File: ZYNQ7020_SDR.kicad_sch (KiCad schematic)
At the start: 0 parts

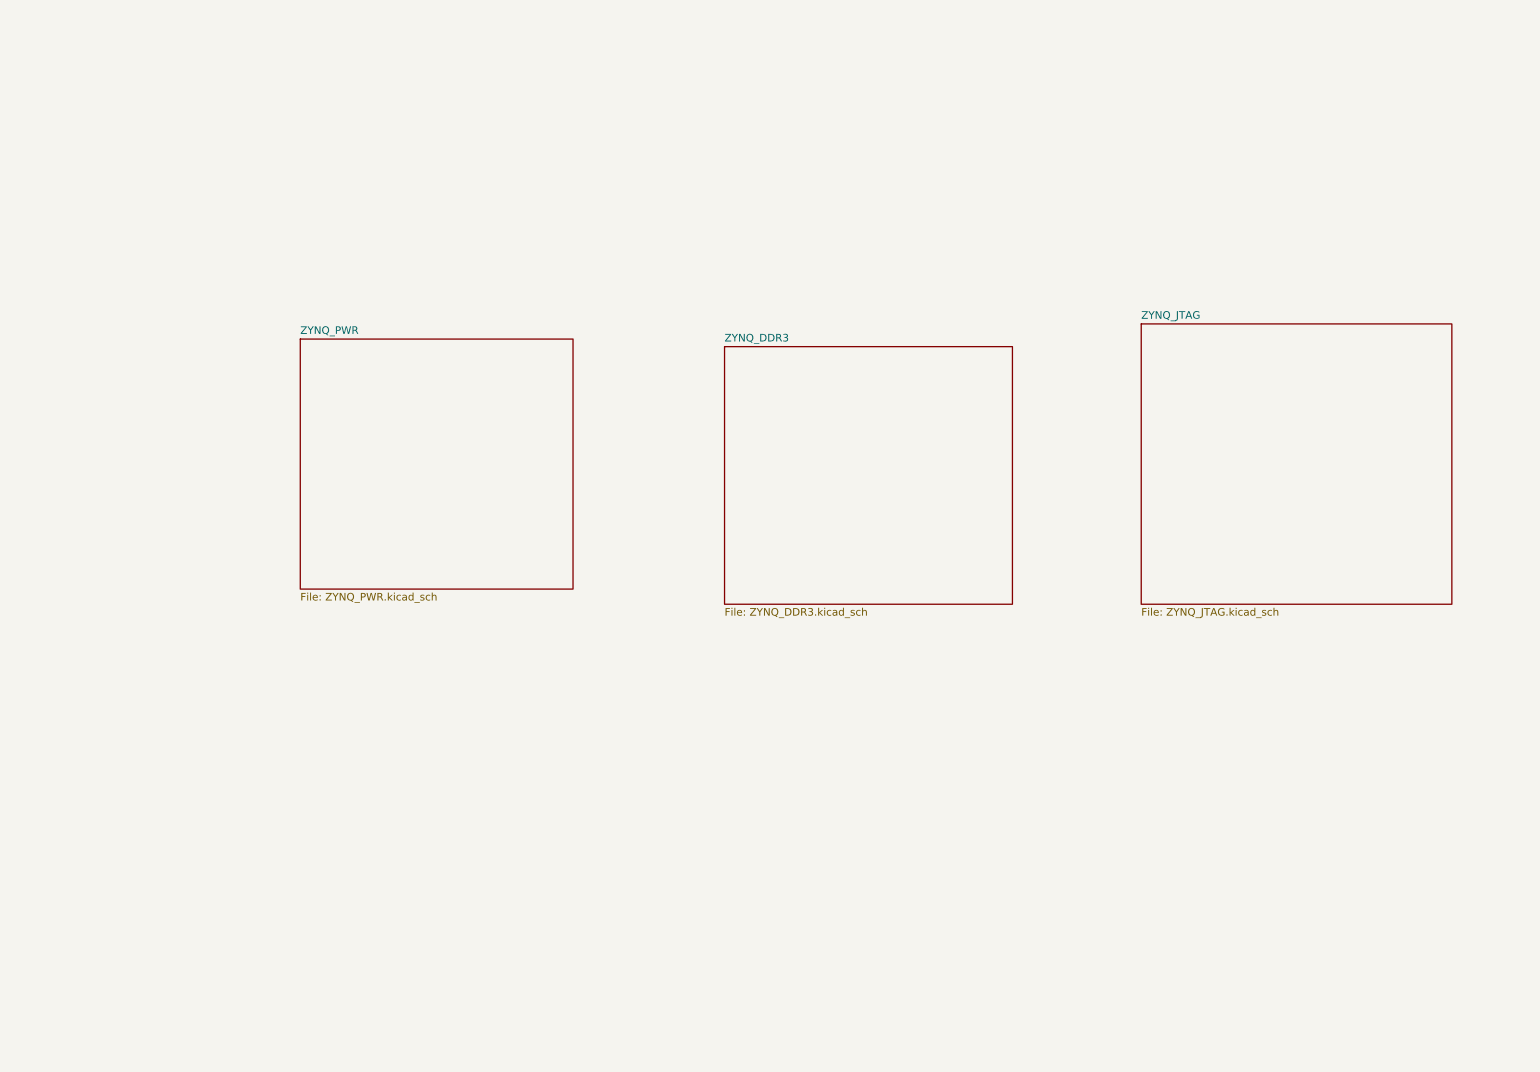
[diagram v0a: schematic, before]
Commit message: Add Bank, Storage, Ethernet and USB schematic sheets
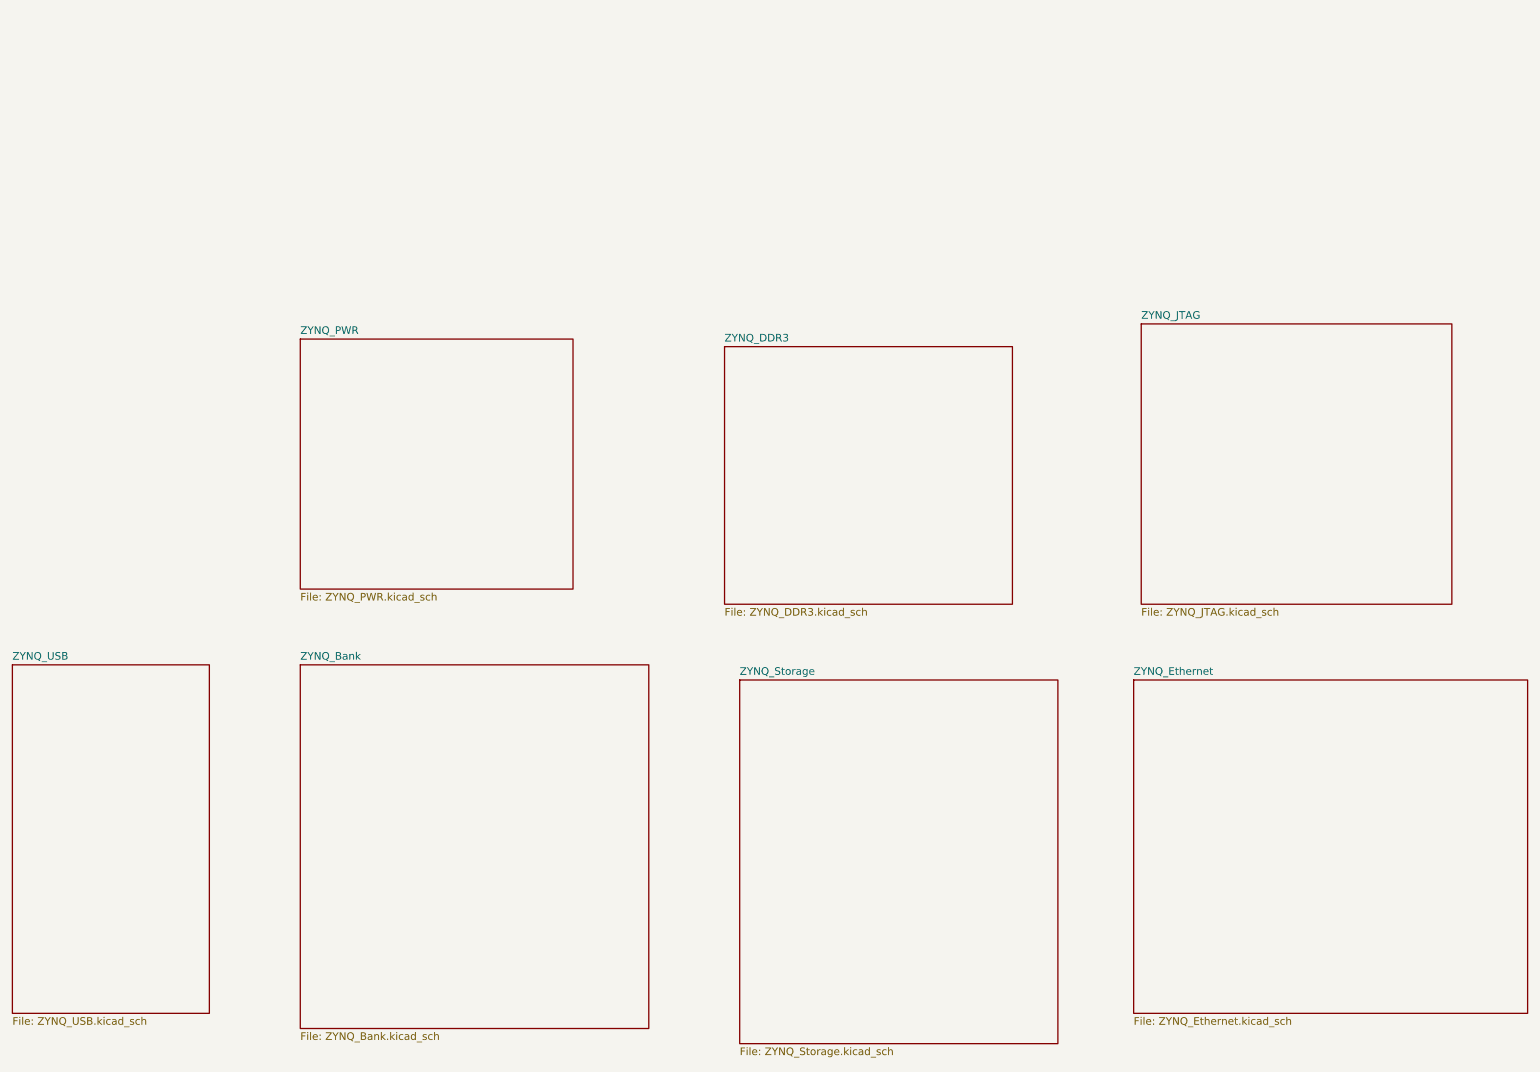
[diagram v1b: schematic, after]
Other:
- added sheet ZYNQ_Bank (ZYNQ_Bank.kicad_sch)
- added sheet ZYNQ_Ethernet (ZYNQ_Ethernet.kicad_sch)
- added sheet ZYNQ_Storage (ZYNQ_Storage.kicad_sch)
- added sheet ZYNQ_USB (ZYNQ_USB.kicad_sch)
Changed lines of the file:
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@@
+	)
+	(sheet
+		(at 12.7 96.52)
+		(size 33.02 58.42)
+		(exclude_from_sim no)
+		(in_bom yes)
+		(on_board yes)
+		(dnp no)
+		(fields_autoplaced yes)
+		(stroke
+			(width 0.1524)
+			(type solid)
+		)
+		(fill
+			(color 0 0 0 0)
+		)
+		(property "Sheetname" "ZYNQ_USB"
+			(at 12.7 95.8084 0)
+			(show_name no)
+			(do_not_autoplace no)
+			(effects
+				(font
+					(size 1.27 1.27)
+				)
+				(justify left bottom)
+			)
+		)
+		(property "Sheetfile" "ZYNQ_USB.kicad_sch"
+			(at 12.7 155.5246 0)
+			(show_name no)
+			(do_not_autoplace no)
+			(effects
+				(font
+					(size 1.27 1.27)
+				)
+				(justify left top)
+			)
+		)
+		(instances
+			(project "ZYNQ7020_SDR"
+				(path "/3a68e3c4-732f-4f36-849e-450e7f6f5412"
+					(page "8")
+				)
+			)
+		)
+	)
+	(sheet
+		(at 60.96 96.52)
+		(size 58.42 60.96)
+		(exclude_from_sim no)
+		(in_bom yes)
+		(on_board yes)
+		(dnp no)
+		(fields_autoplaced yes)
+		(stroke
+			(width 0.1524)
+			(type solid)
+		)
+		(fill
+			(color 0 0 0 0)
+		)
+		(property "Sheetname" "ZYNQ_Bank"
+			(at 60.96 95.8084 0)
+			(show_name no)
+			(do_not_autoplace no)
+			(effects
+				(font
+					(size 1.27 1.27)
+				)
+				(justify left bottom)
+			)
+		)
+		(property "Sheetfile" "ZYNQ_Bank.kicad_sch"
+			(at 60.96 158.0646 0)
+			(show_name no)
+			(do_not_autoplace no)
+			(effects
+				(font
+					(size 1.27 1.27)
+				)
+				(justify left top)
+			)
+		)
+		(instances
+			(project "ZYNQ7020_SDR"
+				(path "/3a68e3c4-732f-4f36-849e-450e7f6f5412"
+					(page "5")
+				)
+			)
+		)
 	)
 	(sheet
@@
 				)
 			)
+		)
+	)
+	(sheet
+		(at 200.66 99.06)
+		(size 66.04 55.88)
+		(exclude_from_sim no)
+		(in_bom yes)
+		(on_board yes)
+		(dnp no)
+		(fields_autoplaced yes)
+		(stroke
+			(width 0.1524)
+			(type solid)
+		)
+		(fill
+			(color 0 0 0 0)
+		)
+		(property "Sheetname" "ZYNQ_Ethernet"
+			(at 200.66 98.3484 0)
+			(show_name no)
+			(do_not_autoplace no)
+			(effects
+				(font
+					(size 1.27 1.27)
+				)
+				(justify left bottom)
+			)
+		)
+		(property "Sheetfile" "ZYNQ_Ethernet.kicad_sch"
+			(at 200.66 155.5246 0)
+			(show_name no)
+			(do_not_autoplace no)
+			(effects
+				(font
+					(size 1.27 1.27)
+				)
+				(justify left top)
+			)
+		)
+		(instances
+			(project "ZYNQ7020_SDR"
+				(path "/3a68e3c4-732f-4f36-849e-450e7f6f5412"
+					(page "7")
+				)
+			)
+		)
+	)
+	(sheet
+		(at 134.62 99.06)
+		(size 53.34 60.96)
+		(exclude_from_sim no)
+		(in_bom yes)
+		(on_board yes)
+		(dnp no)
+		(fields_autoplaced yes)
+		(stroke
+			(width 0.1524)
+			(type solid)
+		)
+		(fill
+			(color 0 0 0 0)
+		)
+		(property "Sheetname" "ZYNQ_Storage"
+			(at 134.62 98.3484 0)
+			(show_name no)
+			(do_not_autoplace no)
+			(effects
+				(font
+					(size 1.27 1.27)
+				)
+				(justify left bottom)
+			)
+		)
+		(property "Sheetfile" "ZYNQ_Storage.kicad_sch"
+			(at 134.62 160.6046 0)
+			(show_name no)
+			(do_not_autoplace no)
+			(effects
+				(font
+					(size 1.27 1.27)
+				)
+				(justify left top)
+			)
+		)
+		(instances
+			(project "ZYNQ7020_SDR"
+				(path "/3a68e3c4-732f-4f36-849e-450e7f6f5412"
+					(page "6")
+				)
+			)

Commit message: Refactor schematic hierarchy and add PL Ethernet
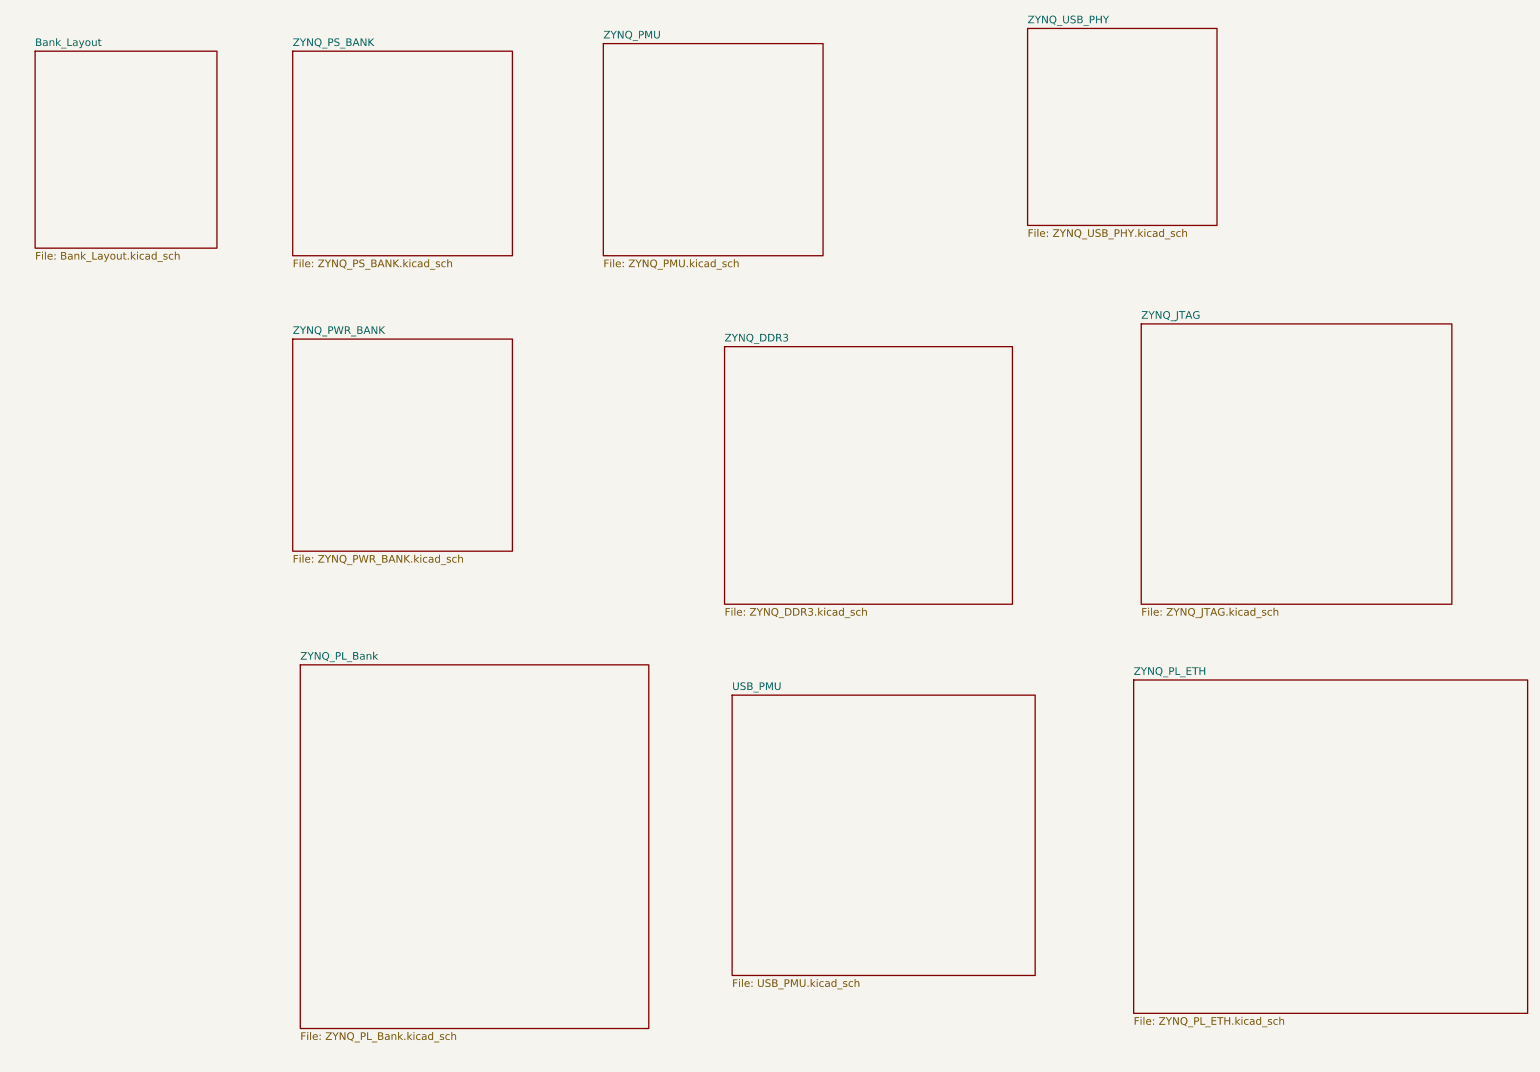
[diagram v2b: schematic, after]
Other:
- sheet ZYNQ_Bank renamed ZYNQ_PL_Bank
- sheet ZYNQ_Ethernet renamed ZYNQ_PL_ETH
- sheet ZYNQ_PWR renamed ZYNQ_PWR_BANK
- removed sheet ZYNQ_Storage
- removed sheet ZYNQ_USB
- added sheet Bank_Layout (Bank_Layout.kicad_sch)
- added sheet USB_PMU (USB_PMU.kicad_sch)
- added sheet ZYNQ_PMU (ZYNQ_PMU.kicad_sch)
- added sheet ZYNQ_PS_BANK (ZYNQ_PS_BANK.kicad_sch)
- added sheet ZYNQ_USB_PHY (ZYNQ_USB_PHY.kicad_sch)
- sheet ZYNQ_PL_Bank: file ZYNQ_Bank.kicad_sch -> ZYNQ_PL_Bank.kicad_sch
- sheet ZYNQ_PL_ETH: file ZYNQ_Ethernet.kicad_sch -> ZYNQ_PL_ETH.kicad_sch
- sheet ZYNQ_PWR_BANK: file ZYNQ_PWR.kicad_sch -> ZYNQ_PWR_BANK.kicad_sch
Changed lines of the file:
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@@
+			(project "ZYNQ7020_SDR"
+				(path "/3a68e3c4-732f-4f36-849e-450e7f6f5412"
+					(page "4")
+				)
+			)
+		)
+	)
+	(sheet
+		(at 133.35 101.6)
+		(size 50.8 46.99)
+		(exclude_from_sim no)
+		(in_bom yes)
+		(on_board yes)
+		(dnp no)
+		(fields_autoplaced yes)
+		(stroke
+			(width 0.1524)
+			(type solid)
+		)
+		(fill
+			(color 0 0 0 0)
+		)
+		(property "Sheetname" "USB_PMU"
+			(at 133.35 100.8884 0)
+			(show_name no)
+			(do_not_autoplace no)
+			(effects
+				(font
+					(size 1.27 1.27)
+				)
+				(justify left bottom)
+			)
+		)
+		(property "Sheetfile" "USB_PMU.kicad_sch"
+			(at 133.35 149.1746 0)
+			(show_name no)
+			(do_not_autoplace no)
+			(effects
+				(font
+					(size 1.27 1.27)
+				)
+				(justify left top)
+			)
+		)
+		(instances
+			(project "ZYNQ7020_SDR"
+				(path "/3a68e3c4-732f-4f36-849e-450e7f6f5412"
+					(page "10")
+				)
+			)
+		)
+	)
+	(sheet
+		(at 59.69 -6.35)
+		(size 36.83 34.29)
+		(exclude_from_sim no)
+		(in_bom yes)
+		(on_board yes)
+		(dnp no)
+		(fields_autoplaced yes)
+		(stroke
+			(width 0.1524)
+			(type solid)
+		)
+		(fill
+			(color 0 0 0 0)
+		)
+		(property "Sheetname" "ZYNQ_PS_BANK"
+			(at 59.69 -7.0616 0)
+			(show_name no)
+			(do_not_autoplace no)
+			(effects
+				(font
+					(size 1.27 1.27)
+				)
+				(justify left bottom)
+			)
+		)
+		(property "Sheetfile" "ZYNQ_PS_BANK.kicad_sch"
+			(at 59.69 28.5246 0)
+			(show_name no)
+			(do_not_autoplace no)
+			(effects
+				(font
+					(size 1.27 1.27)
+				)
+				(justify left top)
+			)
+		)
+		(instances
+			(project "ZYNQ7020_SDR"
+				(path "/3a68e3c4-732f-4f36-849e-450e7f6f5412"
+					(page "7")
+				)
+			)
+		)
+	)
+	(sheet
+		(at 111.76 -7.62)
+		(size 36.83 35.56)
+		(exclude_from_sim no)
+		(in_bom yes)
+		(on_board yes)
+		(dnp no)
+		(fields_autoplaced yes)
+		(stroke
+			(width 0.1524)
+			(type solid)
+		)
+		(fill
+			(color 0 0 0 0)
+		)
+		(property "Sheetname" "ZYNQ_PMU"
+			(at 111.76 -8.3316 0)
+			(show_name no)
+			(do_not_autoplace no)
+			(effects
+				(font
+					(size 1.27 1.27)
+				)
+				(justify left bottom)
+			)
+		)
+		(property "Sheetfile" "ZYNQ_PMU.kicad_sch"
+			(at 111.76 28.5246 0)
+			(show_name no)
+			(do_not_autoplace no)
+			(effects
+				(font
+					(size 1.27 1.27)
+				)
+				(justify left top)
+			)
+		)
+		(instances
 			(project "ZYNQ7020_SDR"
 				(path "/3a68e3c4-732f-4f36-849e-450e7f6f5412"
@@
 	)
 	(sheet
-		(at 12.7 96.52)
-		(size 33.02 58.42)
-		(exclude_from_sim no)
-		(in_bom yes)
-		(on_board yes)
-		(dnp no)
-		(fields_autoplaced yes)
-		(stroke
-			(width 0.1524)
-			(type solid)
-		)
-		(fill
-			(color 0 0 0 0)
-		)
-		(property "Sheetname" "ZYNQ_USB"
-			(at 12.7 95.8084 0)
-			(show_name no)
-			(do_not_autoplace no)
-			(effects
-				(font
-					(size 1.27 1.27)
-				)
-				(justify left bottom)
-			)
-		)
-		(property "Sheetfile" "ZYNQ_USB.kicad_sch"
-			(at 12.7 155.5246 0)
-			(show_name no)
-			(do_not_autoplace no)
-			(effects
-				(font
-					(size 1.27 1.27)
-				)
-				(justify left top)
-			)
-		)
-		(instances
-			(project "ZYNQ7020_SDR"
-				(path "/3a68e3c4-732f-4f36-849e-450e7f6f5412"
-					(page "8")
+		(at 16.51 -6.35)
+		(size 30.48 33.02)
+		(exclude_from_sim no)
+		(in_bom yes)
+		(on_board yes)
+		(dnp no)
+		(fields_autoplaced yes)
+		(stroke
+			(width 0.1524)
+			(type solid)
+		)
+		(fill
+			(color 0 0 0 0)
+		)
+		(property "Sheetname" "Bank_Layout"
+			(at 16.51 -7.0616 0)
+			(show_name no)
+			(do_not_autoplace no)
+			(effects
+				(font
+					(size 1.27 1.27)
+				)
+				(justify left bottom)
+			)
+		)
+		(property "Sheetfile" "Bank_Layout.kicad_sch"
+			(at 16.51 27.2546 0)
+			(show_name no)
+			(do_not_autoplace no)
+			(effects
+				(font
+					(size 1.27 1.27)
+				)
+				(justify left top)
+			)
+		)
+		(instances
+			(project "ZYNQ7020_SDR"
+				(path "/3a68e3c4-732f-4f36-849e-450e7f6f5412"
+					(page "2")
 				)
 			)
@@
 			(color 0 0 0 0)
 		)
-		(property "Sheetname" "ZYNQ_Bank"
+		(property "Sheetname" "ZYNQ_PL_Bank"
 			(at 60.96 95.8084 0)
 			(show_name no)
@@
 			)
 		)
-		(property "Sheetfile" "ZYNQ_Bank.kicad_sch"
+		(property "Sheetfile" "ZYNQ_PL_Bank.kicad_sch"
 			(at 60.96 158.0646 0)
 			(show_name no)
@@
 	)
 	(sheet
-		(at 60.96 41.91)
-		(size 45.72 41.91)
-		(exclude_from_sim no)
-		(in_bom yes)
-		(on_board yes)
-		(dnp no)
-		(fields_autoplaced yes)
-		(stroke
-			(width 0.1524)
-			(type solid)
-		)
-		(fill
-			(color 0 0 0 0)
-		)
-		(property "Sheetname" "ZYNQ_PWR"
-			(at 60.96 41.1984 0)
-			(show_name no)
-			(do_not_autoplace no)
-			(effects
-				(font
-					(size 1.27 1.27)
-				)
-				(justify left bottom)
-			)
-		)
-		(property "Sheetfile" "ZYNQ_PWR.kicad_sch"
-			(at 60.96 84.4046 0)
-			(show_name no)
-			(do_not_autoplace no)
-			(effects
-				(font
-					(size 1.27 1.27)
-				)
-				(justify left top)
-			)
-		)
-		(instances
-			(project "ZYNQ7020_SDR"
-				(path "/3a68e3c4-732f-4f36-849e-450e7f6f5412"
-					(page "2")
+		(at 59.69 41.91)
+		(size 36.83 35.56)
+		(exclude_from_sim no)
+		(in_bom yes)
+		(on_board yes)
+		(dnp no)
+		(fields_autoplaced yes)
+		(stroke
+			(width 0.1524)
+			(type solid)
+		)
+		(fill
+			(color 0 0 0 0)
+		)
+		(property "Sheetname" "ZYNQ_PWR_BANK"
+			(at 59.69 41.1984 0)
+			(show_name no)
+			(do_not_autoplace no)
+			(effects
+				(font
+					(size 1.27 1.27)
+				)
+				(justify left bottom)
+			)
+		)
+		(property "Sheetfile" "ZYNQ_PWR_BANK.kicad_sch"
+			(at 59.69 78.0546 0)
+			(show_name no)
+			(do_not_autoplace no)
+			(effects
+				(font
+					(size 1.27 1.27)
+				)
+				(justify left top)
+			)
+		)
+		(instances
+			(project "ZYNQ7020_SDR"
+				(path "/3a68e3c4-732f-4f36-849e-450e7f6f5412"
+					(page "4")
 				)
 			)
@@
 			(color 0 0 0 0)
 		)
-		(property "Sheetname" "ZYNQ_Ethernet"
+		(property "Sheetname" "ZYNQ_PL_ETH"
 			(at 200.66 98.3484 0)
 			(show_name no)
@@
 			)
 		)
-		(property "Sheetfile" "ZYNQ_Ethernet.kicad_sch"
+		(property "Sheetfile" "ZYNQ_PL_ETH.kicad_sch"
 			(at 200.66 155.5246 0)
 			(show_name no)
@@
 			(project "ZYNQ7020_SDR"
 				(path "/3a68e3c4-732f-4f36-849e-450e7f6f5412"
-					(page "7")
-				)
-			)
-		)
-	)
-	(sheet
-		(at 134.62 99.06)
-		(size 53.34 60.96)
-		(exclude_from_sim no)
-		(in_bom yes)
-		(on_board yes)
-		(dnp no)
-		(fields_autoplaced yes)
-		(stroke
-			(width 0.1524)
-			(type solid)
-		)
-		(fill
-			(color 0 0 0 0)
-		)
-		(property "Sheetname" "ZYNQ_Storage"
-			(at 134.62 98.3484 0)
-			(show_name no)
-			(do_not_autoplace no)
-			(effects
-				(font
-					(size 1.27 1.27)
-				)
-				(justify left bottom)
-			)
-		)
-		(property "Sheetfile" "ZYNQ_Storage.kicad_sch"
-			(at 134.62 160.6046 0)
-			(show_name no)
-			(do_not_autoplace no)
-			(effects
-				(font
-					(size 1.27 1.27)
-				)
-				(justify left top)
-			)
-		)
-		(instances
-			(project "ZYNQ7020_SDR"
-				(path "/3a68e3c4-732f-4f36-849e-450e7f6f5412"
 					(page "6")
 				)
 			)
+		)
+	)
+	(sheet
+		(at 182.88 -10.16)
+		(size 31.75 33.02)
+		(exclude_from_sim no)
+		(in_bom yes)
+		(on_board yes)
+		(dnp no)
+		(fields_autoplaced yes)
+		(stroke
+			(width 0.1524)
+			(type solid)
+		)
+		(fill
+			(color 0 0 0 0)
+		)
+		(property "Sheetname" "ZYNQ_USB_PHY"
+			(at 182.88 -10.8716 0)
+			(show_name no)
+			(do_not_autoplace no)
+			(effects
+				(font
+					(size 1.27 1.27)
+				)
+				(justify left bottom)
+			)
+		)
+		(property "Sheetfile" "ZYNQ_USB_PHY.kicad_sch"
+			(at 182.88 23.4446 0)
+			(show_name no)
+			(do_not_autoplace no)
+			(effects
+				(font
+					(size 1.27 1.27)
+				)
+				(justify left top)
+			)
+		)
+		(instances
+			(project "ZYNQ7020_SDR"
+				(path "/3a68e3c4-732f-4f36-849e-450e7f6f5412"
+					(page "9")
+				)
+			)

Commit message: Update JTAG and SDR schematics and libraries
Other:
- sheet ZYNQ_PL_ETH renamed ZYNQ_PS_ETH
- sheet ZYNQ_PS_ETH: file ZYNQ_PL_ETH.kicad_sch -> ZYNQ_PS_ETH.kicad_sch
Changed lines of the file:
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@@
 			(project "ZYNQ7020_SDR"
 				(path "/3a68e3c4-732f-4f36-849e-450e7f6f5412"
-					(page "4")
+					(page "8")
 				)
 			)
@@
 			(project "ZYNQ7020_SDR"
 				(path "/3a68e3c4-732f-4f36-849e-450e7f6f5412"
-					(page "10")
+					(page "12")
 				)
 			)
@@
 			(project "ZYNQ7020_SDR"
 				(path "/3a68e3c4-732f-4f36-849e-450e7f6f5412"
-					(page "4")
+					(page "11")
 				)
 			)
@@
 			(color 0 0 0 0)
 		)
-		(property "Sheetname" "ZYNQ_PL_ETH"
+		(property "Sheetname" "ZYNQ_PS_ETH"
 			(at 200.66 98.3484 0)
 			(show_name no)
@@
 			)
 		)
-		(property "Sheetfile" "ZYNQ_PL_ETH.kicad_sch"
+		(property "Sheetfile" "ZYNQ_PS_ETH.kicad_sch"
 			(at 200.66 155.5246 0)
 			(show_name no)
